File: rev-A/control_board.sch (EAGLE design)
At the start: 126 parts, among them IC1 W5500, IC3 ATMEGA32U4-AU, J1 USB_B_PTH, K1 G5V1, K2 G5V1, K3 G5V1, SW1 SPST_TACT-KMR2, Y1 8MHz, Y2 25MHz, 10pF

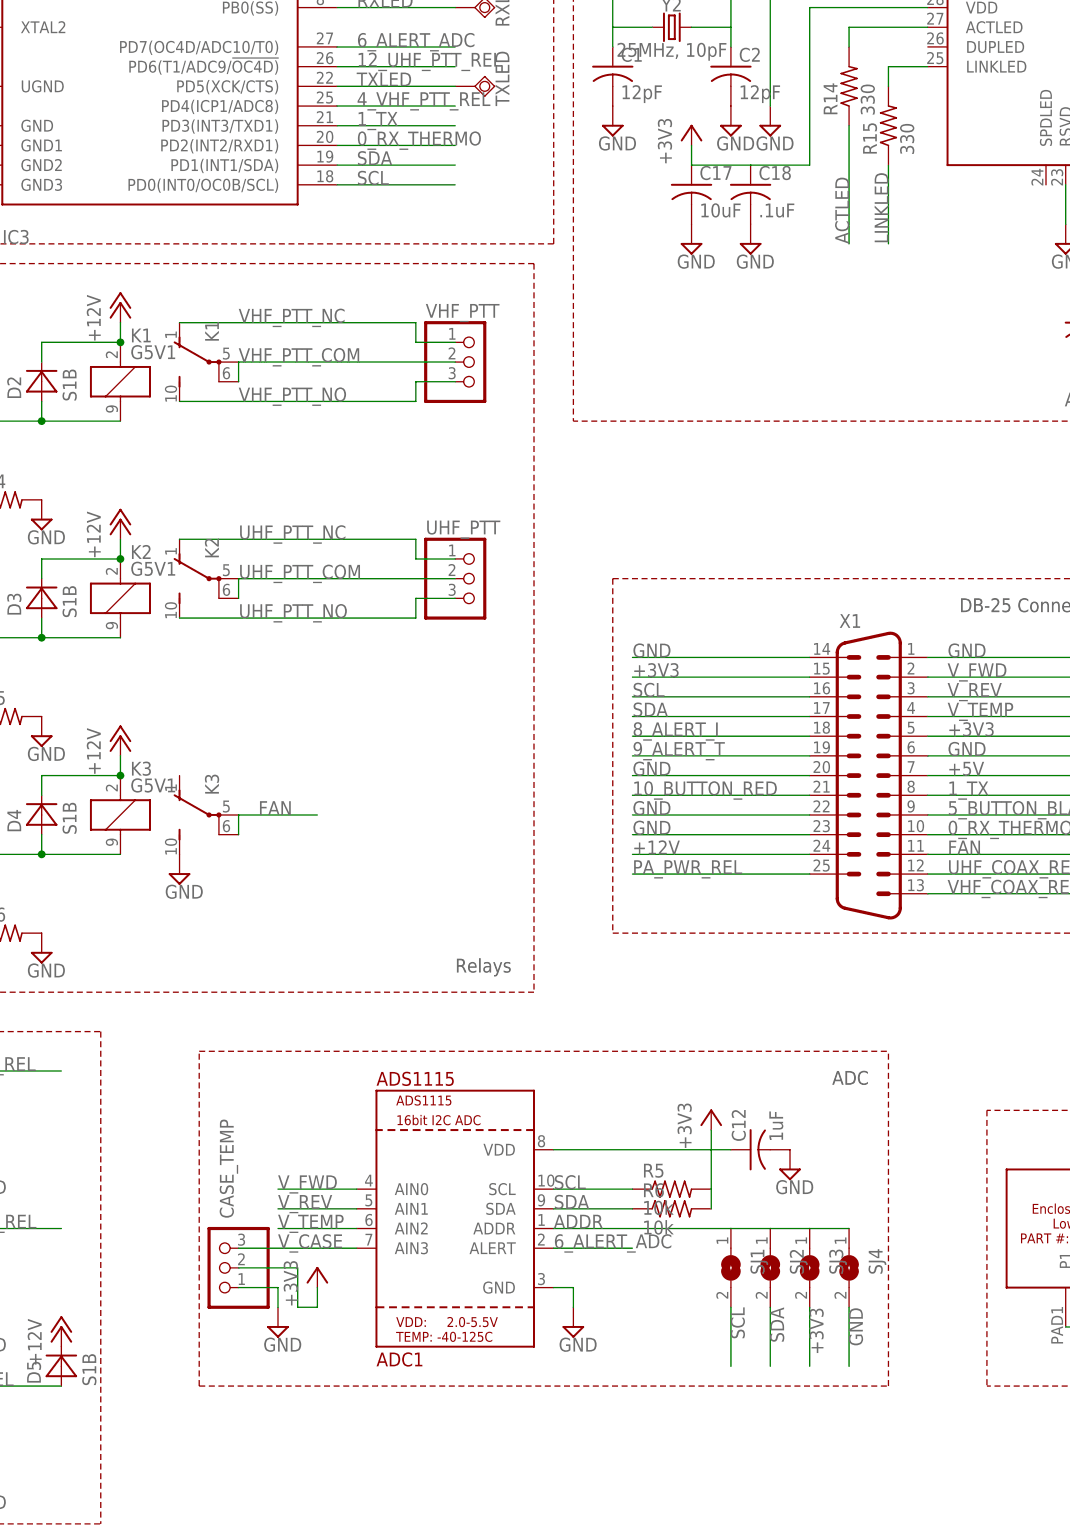
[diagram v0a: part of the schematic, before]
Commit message: lots of updates, added caps for ADC, swapped out 5v vreg, moved a lot of parts around, added flyback diodes to relays.
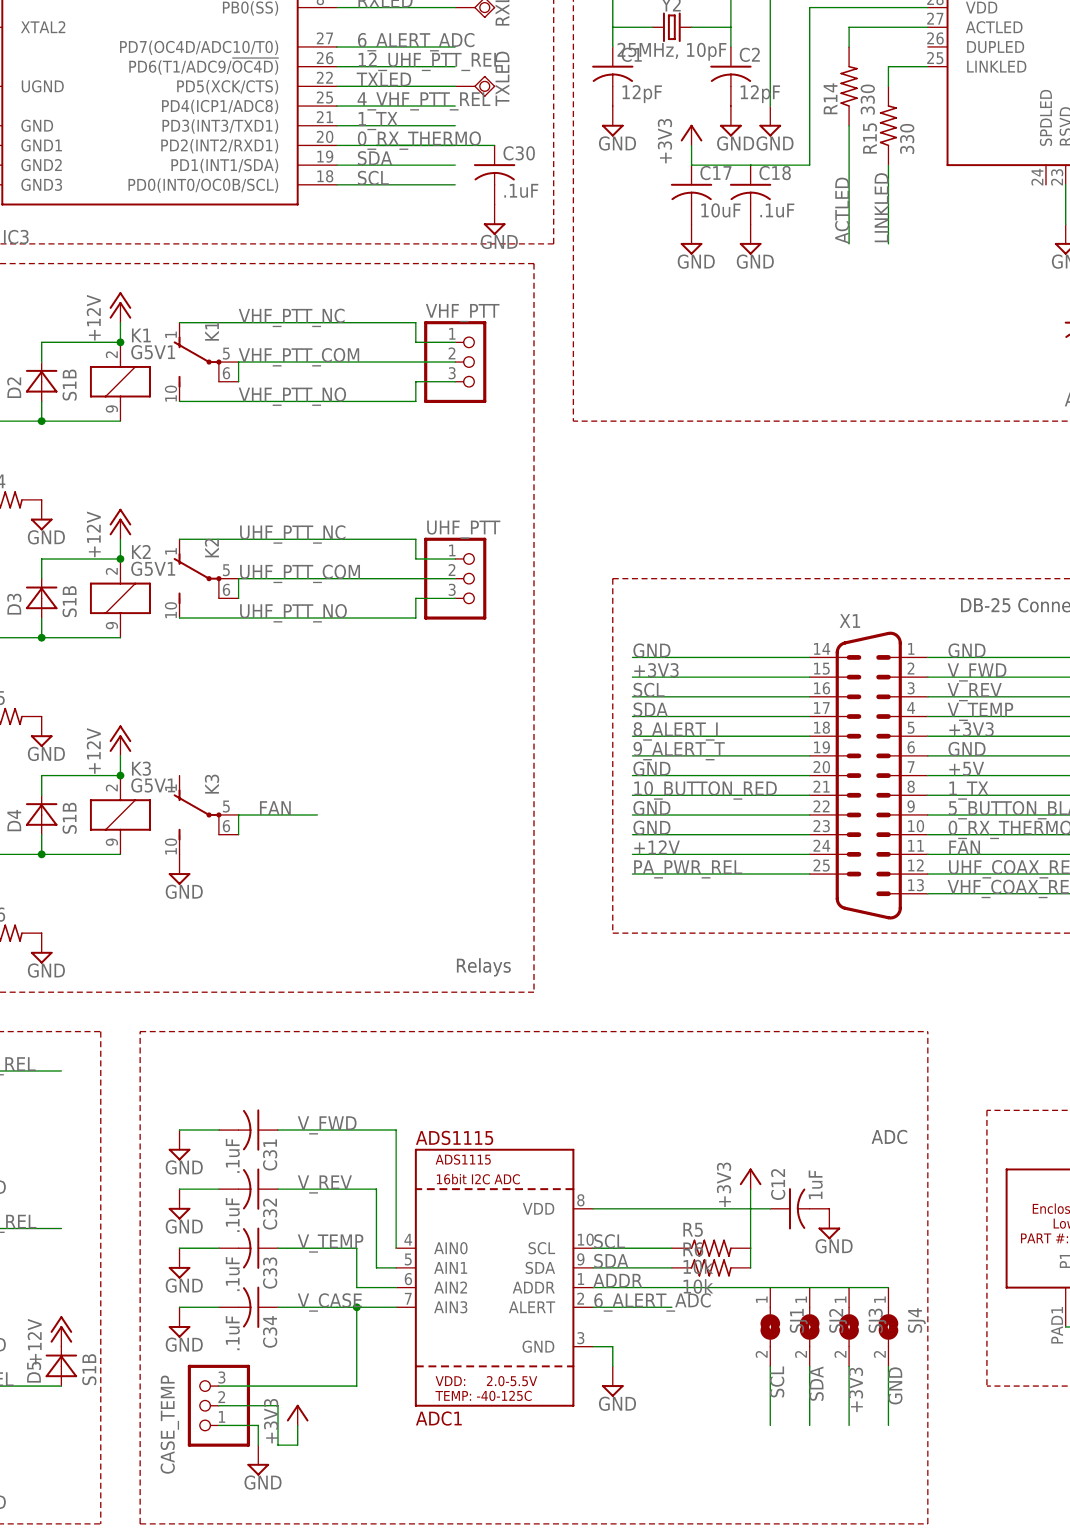
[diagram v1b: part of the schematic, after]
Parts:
- added C30, C31, C32, C33, C34: .1uF, rcl:C-USC0805K
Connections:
- net 0_RX_THERMO: now also C30.1
- net GND: now also C30.2, C31.2, C32.2, C33.2, C34.2
- net V_CASE: now also C34.1
- net V_FWD: now also C31.1
- net V_REV: now also C32.1
- net V_TEMP: now also C33.1
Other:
- moved on the sheet: ADC1, C12, CASE_TEMP, R5, R6, SJ1, SJ2, SJ3, SJ4

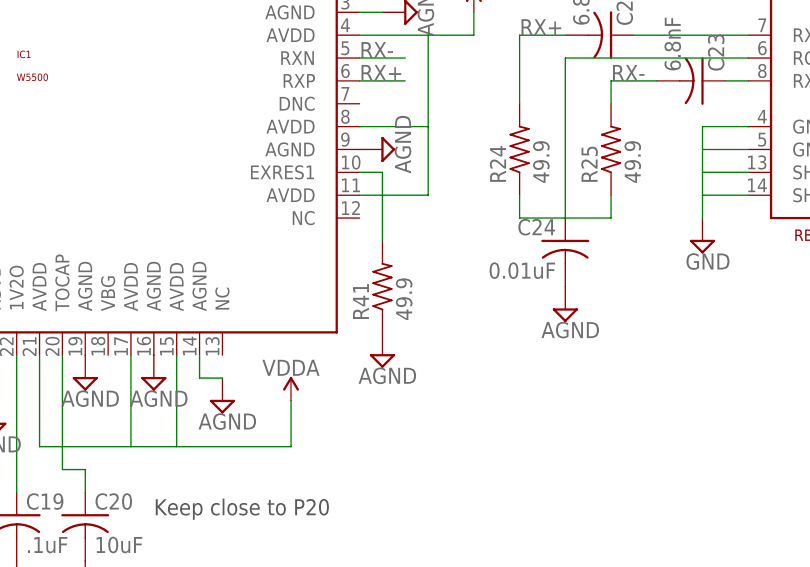
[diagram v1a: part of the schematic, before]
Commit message: fixed R41 value to 12.4k
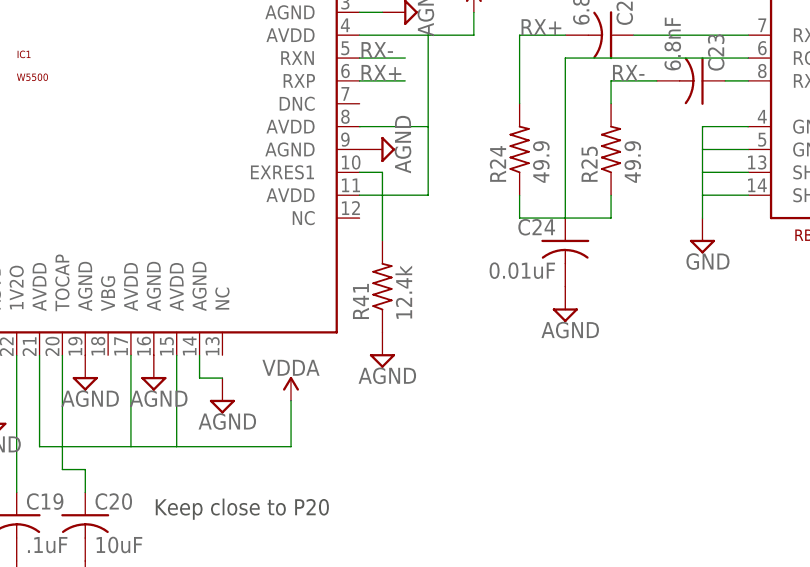
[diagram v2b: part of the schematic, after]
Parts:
- R41: value 49.9 -> 12.4k
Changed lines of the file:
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@@
 <part name="+3V18" library="supply1" library_urn="urn:adsk.eagle:library:371" deviceset="+3V3" device=""/>
 <part name="SUPPLY57" library="supply2" library_urn="urn:adsk.eagle:library:372" deviceset="GND" device=""/>
-<part name="R41" library="rcl" library_urn="urn:adsk.eagle:library:334" deviceset="R-US_" device="R0805" package3d_urn="urn:adsk.eagle:package:23553/2" value="49.9"/>
+<part name="R41" library="rcl" library_urn="urn:adsk.eagle:library:334" deviceset="R-US_" device="R0805" package3d_urn="urn:adsk.eagle:package:23553/2" value="12.4k"/>
 <part name="SUPPLY54" library="supply2" library_urn="urn:adsk.eagle:library:372" deviceset="AGND" device=""/>
 <part name="D2" library="kj4qlp" deviceset="S1B" device=""/>
